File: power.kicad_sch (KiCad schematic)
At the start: 84 parts, among them Q1 PJE138K, Q2 PJE138K, Q3 SSM3J332R, Q4 PJE138K, Q5 SSM3J332R, Q6 PJE138K, Q7 SSM3J332R, U1 TLV70018_SC70, U4 TPS65150PWP, U5 MPQ7235GQBE, U6 TLV76701_WSON6

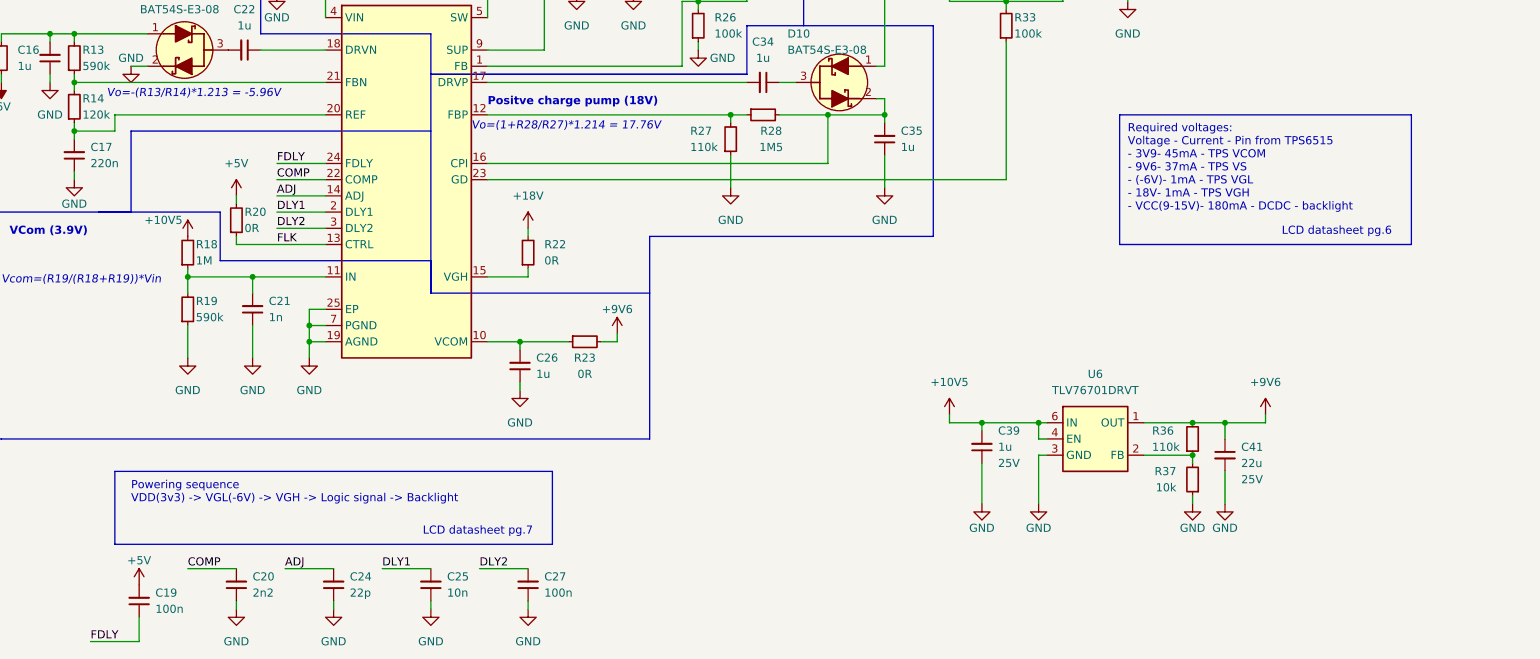
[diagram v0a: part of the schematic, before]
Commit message: [#54932] Change information regarding used display
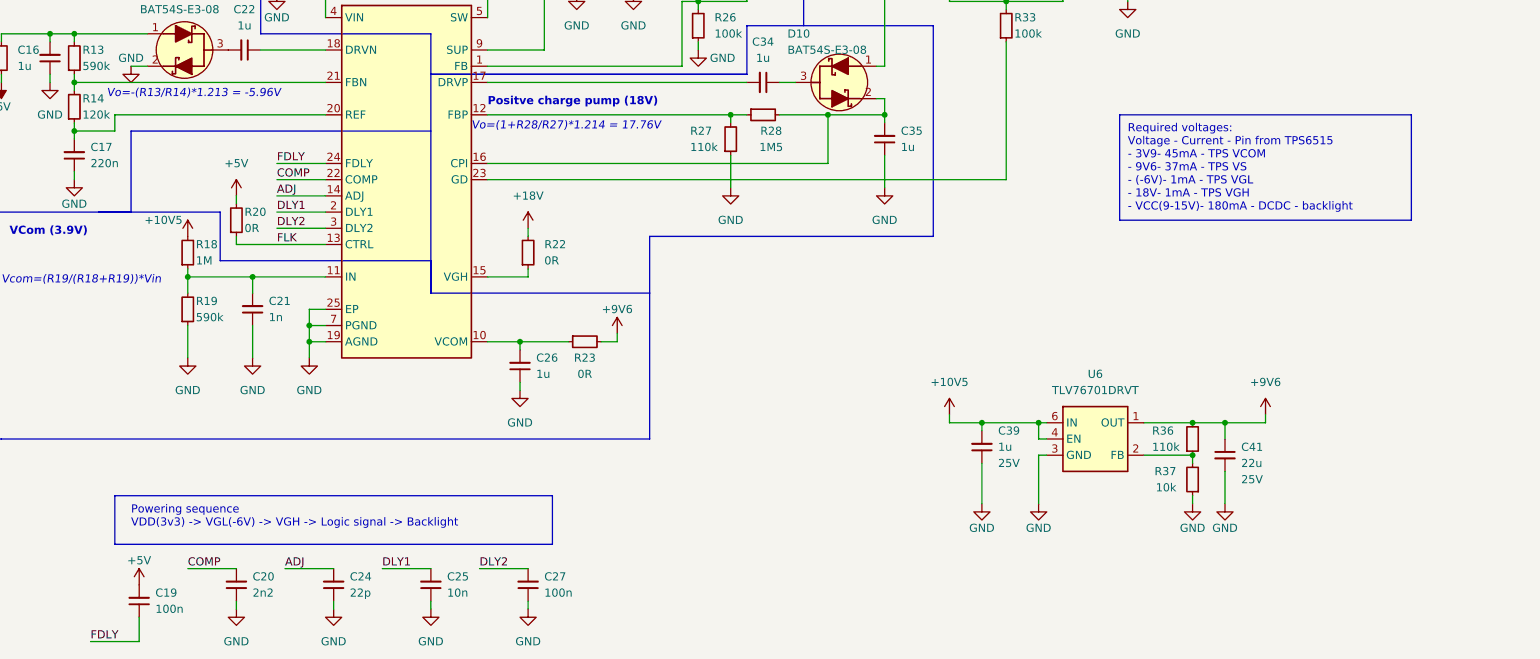
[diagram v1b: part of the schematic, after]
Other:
- note removed: "LCD datasheet pg.6"
- note removed: "LCD datasheet pg.7"
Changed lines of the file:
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@@
     (stroke (width 0) (type default))
   )
-  (polyline (pts (xy 147.32 135.89) (xy 147.32 147.32))
+  (polyline (pts (xy 147.32 139.7) (xy 147.32 147.32))
     (stroke (width 0) (type default))
   )
@@
     (stroke (width 0) (type default))
   )
-  (polyline (pts (xy 350.52 100.33) (xy 350.52 80.01))
+  (polyline (pts (xy 350.52 96.52) (xy 350.52 80.01))
     (stroke (width 0) (type default))
   )
@@
     (stroke (width 0) (type default))
   )
-  (polyline (pts (xy 304.8 100.33) (xy 350.52 100.33))
+  (polyline (pts (xy 304.8 96.52) (xy 350.52 96.52))
     (stroke (width 0) (type default))
   )
@@
     (stroke (width 0) (type default))
   )
-  (polyline (pts (xy 304.8 80.01) (xy 304.8 100.33))
+  (polyline (pts (xy 304.8 80.01) (xy 304.8 96.52))
     (stroke (width 0) (type default))
   )
@@
     (stroke (width 0) (type default))
   )
-  (polyline (pts (xy 215.9 135.89) (xy 215.9 147.32))
+  (polyline (pts (xy 215.9 139.7) (xy 215.9 147.32))
     (stroke (width 0) (type default))
   )
@@
     (stroke (width 0) (type default))
   )
-  (polyline (pts (xy 147.32 135.89) (xy 215.9 135.89))
+  (polyline (pts (xy 147.32 139.7) (xy 215.9 139.7))
     (stroke (width 0) (type default))
   )
@@
     (effects (font (size 1.27 1.27) bold) (justify left bottom))
   )
-  (text "LCD datasheet pg.6\n" (at 330.2 99.06 0)
-    (effects (font (size 1.27 1.27)) (justify left bottom))
-  )
   (text "Vo=(1+R25/R26)*1.146 = 10.54V\n" (at 220.98 52.07 0)
     (effects (font (size 1.27 1.27) italic) (justify left bottom))
   )
   (text "Powering sequence\nVDD(3v3) -> VGL(-6V) -> VGH -> Logic signal -> Backlight "
-    (at 149.86 140.97 0)
+    (at 149.86 144.78 0)
     (effects (font (size 1.27 1.27)) (justify left bottom))
   )
@@
     (effects (font (size 1.27 1.27) (thickness 0.254) bold) (justify left bottom))
   )
-  (text "LCD datasheet pg.7\n" (at 195.58 146.05 0)
-    (effects (font (size 1.27 1.27)) (justify left bottom))
-  )
   (text "Backlight should be set to 180mA CC (voltage from 8.55 to 10.65)\n"

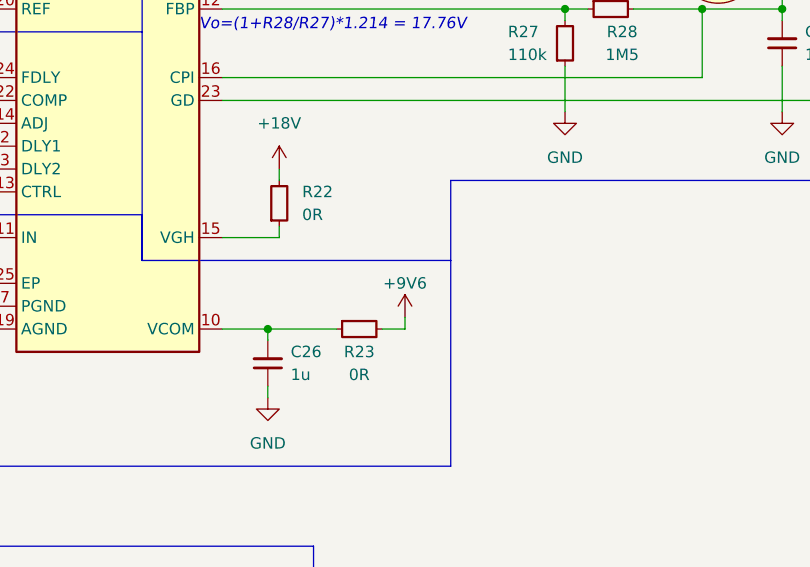
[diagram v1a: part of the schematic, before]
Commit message: [#55272] Route signals
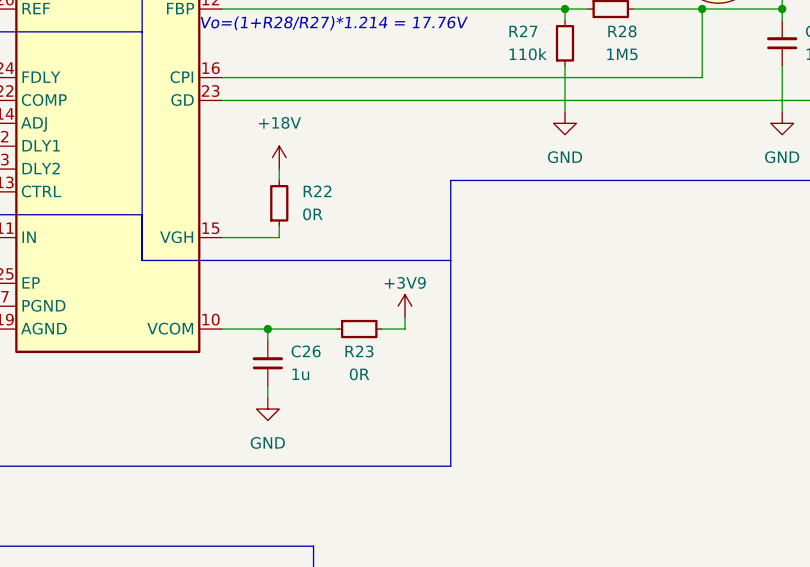
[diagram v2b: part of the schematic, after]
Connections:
- net +9V6: no longer R23.2
- new net +3V9: R23.2
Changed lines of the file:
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@@
+    )
+  )
+  (symbol (lib_id "antmicropower:+3V9") (at 226.06 114.3 0) (unit 1)
+    (in_bom yes) (on_board yes) (dnp no)
+    (property "Reference" "#PWR0121" (at 241.3 114.3 0)
+      (effects (font (size 1.27 1.27) (thickness 0.15)) (justify left bottom) hide)
+    )
+    (property "Value" "+3V9" (at 226.06 110.49 0)
+      (effects (font (size 1.27 1.27) (thickness 0.15)))
+    )
+    (property "Footprint" "" (at 241.3 121.92 0)
+      (effects (font (size 1.27 1.27) (thickness 0.15)) (justify left bottom) hide)
+    )
+    (property "Datasheet" "" (at 241.3 124.46 0)
+      (effects (font (size 1.27 1.27) (thickness 0.15)) (justify left bottom) hide)
+    )
+    (property "Author" "Antmicro" (at 241.3 116.84 0)
+      (effects (font (size 1.27 1.27) (thickness 0.15)) (justify left bottom) hide)
+    )
+    (property "License" "Apache-2.0" (at 241.3 119.38 0)
+      (effects (font (size 1.27 1.27) (thickness 0.15)) (justify left bottom) hide)
+    )
+    (pin "1")
+    (instances
+      (project "cm4-lvds-adapter"
+        (path "/60b842dc-0853-4a25-99ac-5784ddf94d0d/08a1e442-f0a3-4779-ba71-f71979b0fc7c"
+          (reference "#PWR0121") (unit 1)
+        )
+      )
     )
   )
@@
         )
       )
-    )
-  )
-  (symbol (lib_id "antmicropower:+9V6") (at 226.06 114.3 0) (unit 1)
-    (in_bom yes) (on_board yes) (dnp no)
-    (property "Reference" "#PWR0121" (at 241.3 114.3 0)
-      (effects (font (size 1.27 1.27) (thickness 0.15)) (justify left bottom) hide)
-    )
-    (property "Value" "+9V6" (at 226.06 110.49 0)
-      (effects (font (size 1.27 1.27) (thickness 0.15)))
-    )
-    (property "Footprint" "" (at 241.3 121.92 0)
-      (effects (font (size 1.27 1.27) (thickness 0.15)) (justify left bottom) hide)
-    )
-    (property "Datasheet" "" (at 241.3 124.46 0)
-      (effects (font (size 1.27 1.27) (thickness 0.15)) (justify left bottom) hide)
-    )
-    (property "Author" "Antmicro" (at 241.3 116.84 0)
-      (effects (font (size 1.27 1.27) (thickness 0.15)) (justify left bottom) hide)
-    )
-    (property "License" "Apache-2.0" (at 241.3 119.38 0)
-      (effects (font (size 1.27 1.27) (thickness 0.15)) (justify left bottom) hide)
-    )
-    (pin "1")
-    (instances
-      (project "cm4-lvds-adapter"
-        (path "/60b842dc-0853-4a25-99ac-5784ddf94d0d/08a1e442-f0a3-4779-ba71-f71979b0fc7c"
-          (reference "#PWR0121") (unit 1)
-        )
-      )

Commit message: [#55272] Route power
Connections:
- net -VLED: now also C38.2
- net GND: no longer C38.2
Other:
- note added: "V_{com}=(R19/(R18+R19))*Vin"
- note removed: "Vcom=(R19/(R18+R19))*Vin"
- moved on the sheet: C38
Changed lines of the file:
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@@
   (junction (at 93.98 219.71) (diameter 0) (color 0 0 0 0)
   )
+  (junction (at 350.52 226.06) (diameter 0) (color 0 0 0 0)
+  )
   (junction (at 115.57 229.87) (diameter 0) (color 0 0 0 0)
   )
@@
     (stroke (width 0) (type default))
   )
-  (wire (pts (xy 350.52 220.98) (xy 350.52 222.25))
+  (wire (pts (xy 350.52 222.885) (xy 350.52 226.06))
     (stroke (width 0) (type default))
   )
@@
     (stroke (width 0) (type default))
   )
-  (wire (pts (xy 350.52 214.63) (xy 350.52 215.9))
+  (wire (pts (xy 350.52 214.63) (xy 350.52 217.805))
     (stroke (width 0) (type default))
   )
@@
     (stroke (width 0) (type default))
   )
-  (wire (pts (xy 340.36 226.06) (xy 367.03 226.06))
+  (wire (pts (xy 340.36 226.06) (xy 350.52 226.06))
     (stroke (width 0) (type default))
   )
@@
     (stroke (width 0) (type default))
   )
+  (wire (pts (xy 350.52 226.06) (xy 367.03 226.06))
+    (stroke (width 0) (type default))
+  )
   (wire (pts (xy 172.72 87.63) (xy 180.34 87.63))
     (stroke (width 0) (type default))
@@
     )
   )
-  (text "Vcom=(R19/(R18+R19))*Vin" (at 129.54 106.68 0)
+  (text "V_{com}=(R19/(R18+R19))*Vin" (at 129.54 106.68 0)
     (effects (font (size 1.27 1.27) italic) (justify left bottom))
   )
@@
     )
   )
-  (symbol (lib_id "antmicropower:GND") (at 350.52 222.25 0) (unit 1)
-    (in_bom yes) (on_board yes) (dnp no)
-    (property "Reference" "#PWR071" (at 359.41 224.79 0)
-      (effects (font (size 1.27 1.27) (thickness 0.15)) (justify left bottom) hide)
-    )
-    (property "Value" "GND" (at 354.33 223.52 0)
-      (effects (font (size 1.27 1.27) (thickness 0.15)))
-    )
-    (property "Footprint" "" (at 359.41 229.87 0)
-      (effects (font (size 1.27 1.27) (thickness 0.15)) (justify left bottom) hide)
-    )
-    (property "Datasheet" "" (at 359.41 234.95 0)
-      (effects (font (size 1.27 1.27) (thickness 0.15)) (justify left bottom) hide)
-    )
-    (property "Author" "Antmicro" (at 359.41 229.87 0)
-      (effects (font (size 1.27 1.27) (thickness 0.15)) (justify left bottom) hide)
-    )
-    (property "License" "Apache-2.0" (at 359.41 232.41 0)
-      (effects (font (size 1.27 1.27) (thickness 0.15)) (justify left bottom) hide)
-    )
-    (pin "1")
-    (instances
-      (project "cm4-lvds-adapter"
-        (path "/60b842dc-0853-4a25-99ac-5784ddf94d0d/08a1e442-f0a3-4779-ba71-f71979b0fc7c"
-          (reference "#PWR071") (unit 1)
-        )
-      )
-    )
-  )
   (symbol (lib_id "antmicroTransistorsFETsMOSFETsSingle:SSM3J332R") (at 234.95 204.47 270) (mirror x) (unit 1)
     (in_bom yes) (on_board yes) (dnp no) (fields_autoplaced)
@@
     )
   )
-  (symbol (lib_id "antmicroCapacitorsmisc:C_22u_25V_0805") (at 350.52 215.9 90) (mirror x) (unit 1)
+  (symbol (lib_id "antmicroCapacitorsmisc:C_22u_25V_0805") (at 350.52 217.805 90) (mirror x) (unit 1)
     (in_bom yes) (on_board yes) (dnp no) (fields_autoplaced)
-    (property "Reference" "C38" (at 353.06 215.9062 90)
+    (property "Reference" "C38" (at 353.06 217.8112 90)
       (effects (font (size 1.27 1.27)) (justify right))
     )
-    (property "Value" "C_22u_25V_0805" (at 354.33 215.9 0)
+    (property "Value" "C_22u_25V_0805" (at 354.33 217.805 0)
       (effects (font (size 1.27 1.27)) (justify left bottom) hide)
     )
-    (property "Footprint" "antmicro-footprints:C_0805_2012Metric" (at 345.44 220.98 0)
+    (property "Footprint" "antmicro-footprints:C_0805_2012Metric" (at 345.44 222.885 0)
       (effects (font (size 1.524 1.524)) (justify left bottom) hide)
     )
-    (property "Datasheet" "https://product.samsungsem.com/mlcc/CL21A226MAYNNN.do" (at 350.52 215.9 0)
+    (property "Datasheet" "https://product.samsungsem.com/mlcc/CL21A226MAYNNN.do" (at 350.52 217.805 0)
       (effects (font (size 1.27 1.27)) (justify left bottom) hide)
     )
-    (property "Manufacturer" "Samsung Electro-Mechanics" (at 340.36 220.98 0)
+    (property "Manufacturer" "Samsung Electro-Mechanics" (at 340.36 222.885 0)
       (effects (font (size 1.524 1.524)) (justify left bottom) hide)
     )
-    (property "MPN" "CL21A226MAYNNNE" (at 342.9 220.98 0)
+    (property "MPN" "CL21A226MAYNNNE" (at 342.9 222.885 0)
       (effects (font (size 1.524 1.524)) (justify left bottom) hide)
     )
-    (property "Val" "22u" (at 353.06 218.4462 90)
+    (property "Val" "22u" (at 353.06 220.3512 90)
       (effects (font (size 1.27 1.27)) (justify right))
     )
-    (property "License" "Apache-2.0" (at 373.38 236.22 0)
+    (property "License" "Apache-2.0" (at 373.38 238.125 0)
       (effects (font (size 1.27 1.27) (thickness 0.15)) (justify left bottom) hide)
     )
-    (property "Author" "Antmicro" (at 375.92 236.22 0)
+    (property "Author" "Antmicro" (at 375.92 238.125 0)
       (effects (font (size 1.27 1.27) (thickness 0.15)) (justify left bottom) hide)
     )
-    (property "Voltage" "25V" (at 353.06 220.9862 90)
+    (property "Voltage" "25V" (at 353.06 222.8912 90)
       (effects (font (size 1.27 1.27)) (justify right))
     )
-    (property "Dielectric" "X5R" (at 381 236.22 0)
+    (property "Dielectric" "X5R" (at 381 238.125 0)
       (effects (font (size 1.27 1.27)) (justify left bottom) hide)
     )

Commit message: [#55272] Clear silkscreen
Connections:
- net -VLED: no longer C38.2
- net GND: now also C38.2
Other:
- moved on the sheet: C38, R34
